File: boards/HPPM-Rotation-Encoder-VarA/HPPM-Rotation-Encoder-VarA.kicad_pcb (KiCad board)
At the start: 2 copper layers, 15 x 31.2 mm, 13 parts, among them J1 CONN, U1 AS5045B, U2 DS9638

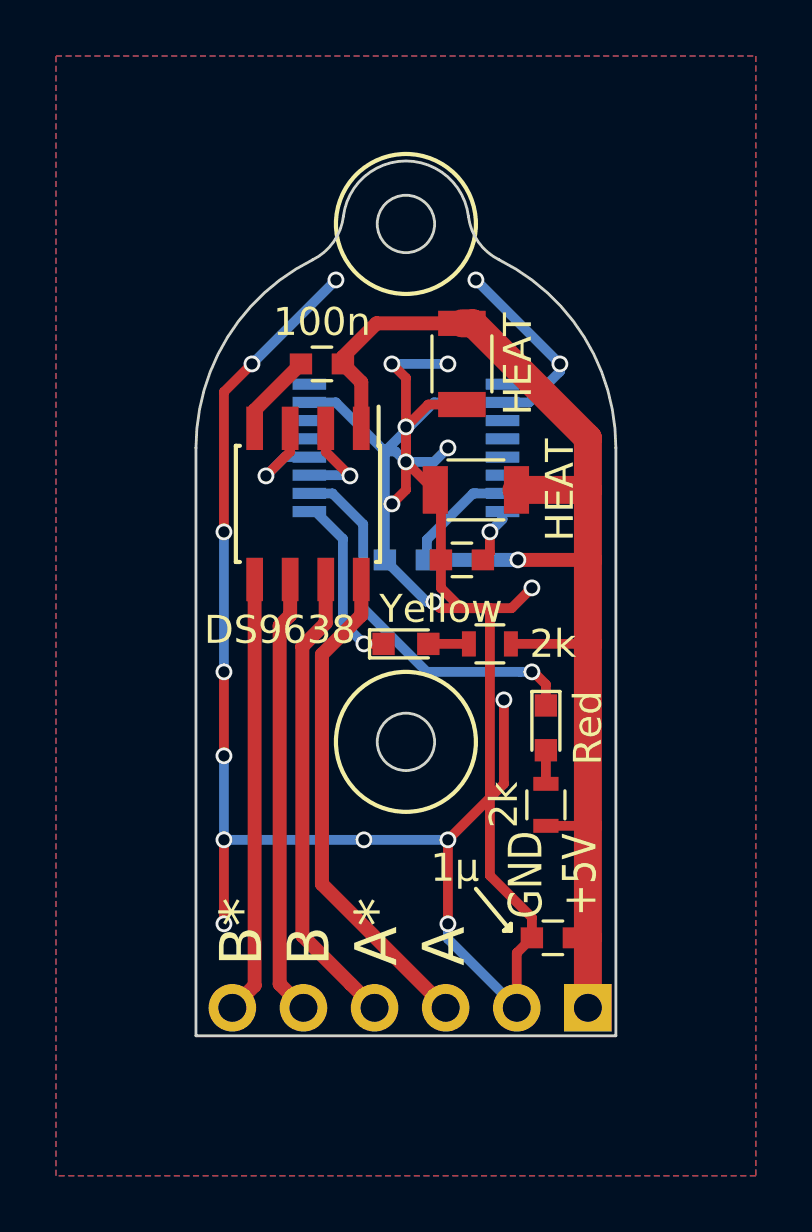
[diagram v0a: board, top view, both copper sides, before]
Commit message: [board][HPPM-Rotation-Encoder-VarA] fix wrong pinout
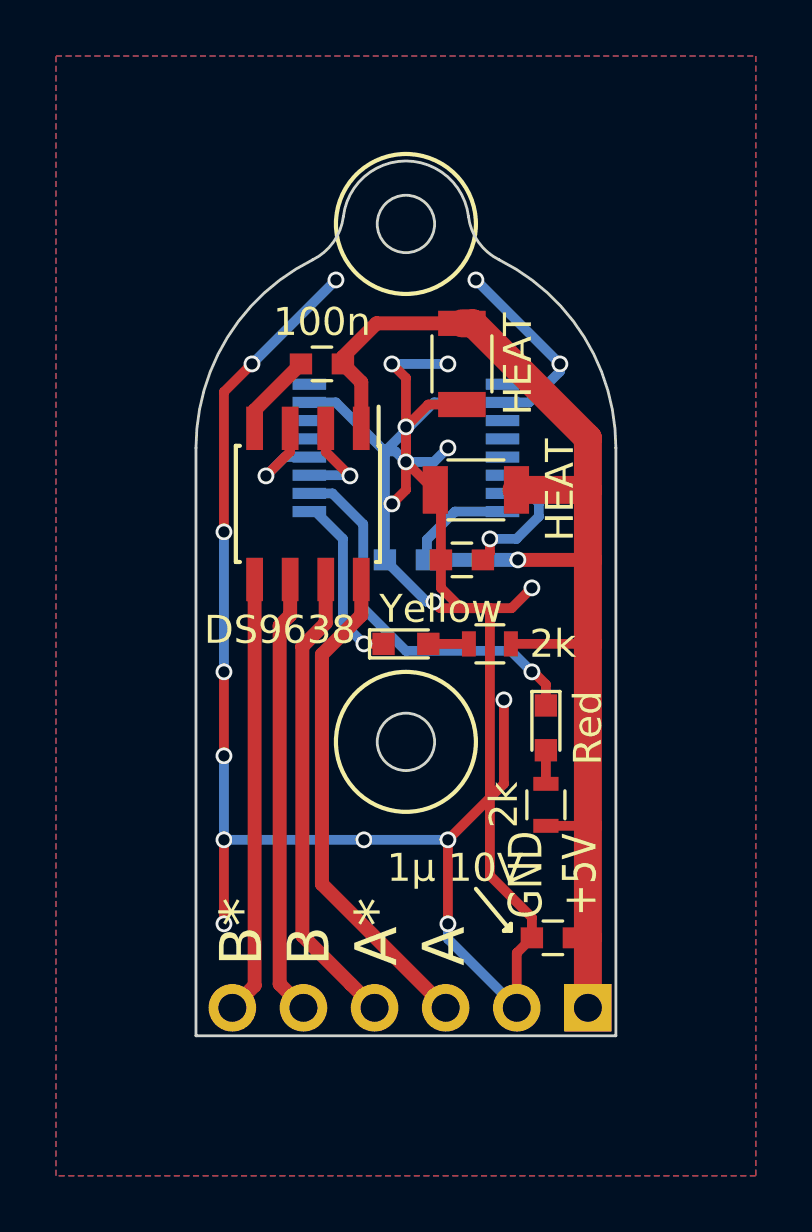
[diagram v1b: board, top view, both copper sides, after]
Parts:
- C4: value 1µ -> 1µ 10V
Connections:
- U1 pad 15: +5V -> Net-(C2-Pad1)
- U1 pad 16: Net-(C2-Pad1) -> +5V
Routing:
- net Net-(C2-Pad1): track 2.01 -> 4.85 mm
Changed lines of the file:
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@@
   (general
     (links 29)
-    (no_connects 0)
+    (no_connects 2)
     (area 49.949999 33.699999 65.050001 65.050001)
     (thickness 1.6)
     (drawings 23)
-    (tracks 150)
+    (tracks 152)
     (zones 0)
     (modules 13)
@@
   )
   (setup
-    (last_trace_width 0.25)
+    (last_trace_width 0.35)
     (user_trace_width 0.35)
     (user_trace_width 0.5)
@@
       (effects (font (size 1 1) (thickness 0.15)))
     )
-    (fp_text value 1µ (at 3.5 2.5 180) (layer F.SilkS)
+    (fp_text value "1µ 10V" (at 3.5 2.5 180) (layer F.SilkS)
       (effects (font (size 1 1) (thickness 0.15)))
     )
@@
     (pad 14 smd rect (at 3.45 0.975) (size 1.2 0.4) (layers B.Cu B.Paste B.Mask))
     (pad 15 smd rect (at 3.45 1.625) (size 1.2 0.4) (layers B.Cu B.Paste B.Mask)
-      (net 1 +5V))
+      (net 3 "Net-(C2-Pad1)"))
     (pad 16 smd rect (at 3.45 2.275) (size 1.2 0.4) (layers B.Cu B.Paste B.Mask)
-      (net 3 "Net-(C2-Pad1)"))
+      (net 1 +5V))
     (model Housings_SSOP.3dshapes/SSOP-16_5.3x6.2mm_Pitch0.65mm.wrl
       (at (xyz 0 0 0))
@@
   (gr_line (start 57.5 44) (end 52.5 44) (layer Dwgs.User) (width 0.1))
   (gr_line (start 50 65) (end 50 44) (layer Edge.Cuts) (width 0.1))
+  (segment (start 60.95 46.275) (end 59.25 46.275) (width 0.35) (layer B.Cu) (net 1))
+  (segment (start 59.25 46.275) (end 58.25 47.275) (width 0.35) (layer B.Cu) (net 1))
+  (segment (start 58.25 47.275) (end 58.25 48) (width 0.35) (layer B.Cu) (net 1))
   (segment (start 61.5 48) (end 58.25 48) (width 0.5) (layer B.Cu) (net 1))
   (via (at 61.5 48) (size 0.6) (drill 0.4) (layers F.Cu B.Cu) (net 1))
@@
   (segment (start 64 51) (end 64 48) (width 1) (layer F.Cu) (net 1))
   (segment (start 64 48) (end 64 45.5) (width 1) (layer F.Cu) (net 1))
-  (segment (start 58.25 48) (end 58.25 47.275) (width 0.35) (layer B.Cu) (net 1))
-  (segment (start 58.25 47.275) (end 59.9 45.625) (width 0.35) (layer B.Cu) (net 1))
-  (segment (start 59.9 45.625) (end 60 45.625) (width 0.35) (layer B.Cu) (net 1))
-  (segment (start 60 45.625) (end 60.95 45.625) (width 0.35) (layer B.Cu) (net 1))
   (segment (start 64 64) (end 64 61.5) (width 1) (layer F.Cu) (net 1))
   (segment (start 64 61.5) (end 64 57.5) (width 1) (layer F.Cu) (net 1))
@@
   (segment (start 52.095 43.3) (end 52.095 42.655) (width 0.5) (layer F.Cu) (net 2))
   (segment (start 52.095 42.655) (end 53.75 41) (width 0.5) (layer F.Cu) (net 2))
-  (segment (start 60.5 47) (end 60.5 47.75) (width 0.35) (layer F.Cu) (net 3))
+  (segment (start 60.5 47.25) (end 60.5 47.75) (width 0.35) (layer F.Cu) (net 3))
   (segment (start 60.5 47.75) (end 60.25 48) (width 0.35) (layer F.Cu) (net 3))
-  (segment (start 60.95 46.275) (end 60.95 46.55) (width 0.35) (layer B.Cu) (net 3))
-  (segment (start 60.95 46.55) (end 60.5 47) (width 0.35) (layer B.Cu) (net 3))
-  (via (at 60.5 47) (size 0.6) (drill 0.4) (layers F.Cu B.Cu) (net 3))
+  (segment (start 62.25 45.975) (end 62.25 46.450002) (width 0.35) (layer B.Cu) (net 3))
+  (segment (start 62.25 46.450002) (end 61.450002 47.25) (width 0.35) (layer B.Cu) (net 3))
+  (segment (start 61.450002 47.25) (end 60.5 47.25) (width 0.35) (layer B.Cu) (net 3))
+  (via (at 60.5 47.25) (size 0.6) (drill 0.4) (layers F.Cu B.Cu) (net 3))
+  (segment (start 60.95 45.625) (end 61.9 45.625) (width 0.35) (layer B.Cu) (net 3))
+  (segment (start 61.9 45.625) (end 62.25 45.975) (width 0.35) (layer B.Cu) (net 3))
   (segment (start 58.3 51) (end 59.75 51) (width 0.35) (layer F.Cu) (net 4))
   (segment (start 54.05 46.275) (end 54.275 46.275) (width 0.35) (layer B.Cu) (net 5))
@@
   (segment (start 54.05 45.625) (end 54.875 45.625) (width 0.35) (layer B.Cu) (net 7))
   (segment (start 54.875 45.625) (end 55.974999 46.724999) (width 0.35) (layer B.Cu) (net 7))
-  (segment (start 58.25 52) (end 61.575736 52) (width 0.35) (layer B.Cu) (net 7))
   (segment (start 55.974999 46.724999) (end 55.974999 49.724999) (width 0.35) (layer B.Cu) (net 7))
-  (segment (start 55.974999 49.724999) (end 58.25 52) (width 0.35) (layer B.Cu) (net 7))
-  (segment (start 61.575736 52) (end 62 52) (width 0.35) (layer B.Cu) (net 7))
+  (segment (start 55.974999 49.724999) (end 57.5 51.25) (width 0.35) (layer B.Cu) (net 7))
+  (segment (start 57.5 51.25) (end 61.25 51.25) (width 0.35) (layer B.Cu) (net 7))
+  (segment (start 61.25 51.25) (end 62 52) (width 0.35) (layer B.Cu) (net 7))
   (segment (start 62.05 52) (end 62 52) (width 0.35) (layer F.Cu) (net 7))
   (segment (start 62.5 52.45) (end 62.05 52) (width 0.35) (layer F.Cu) (net 7))
@@
     (min_thickness 0.25)
     (keepout (tracks not_allowed) (vias not_allowed) (copperpour not_allowed))
-    (fill (arc_segments 16) (thermal_gap 0.25) (thermal_bridge_width 0.3))
+    (fill yes (arc_segments 16) (thermal_gap 0.25) (thermal_bridge_width 0.3))
     (polygon
       (pts

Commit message: [board][HPPM-Rotation-Encoder-Var*] minor fiixes: DRC and PDIO wired to GND
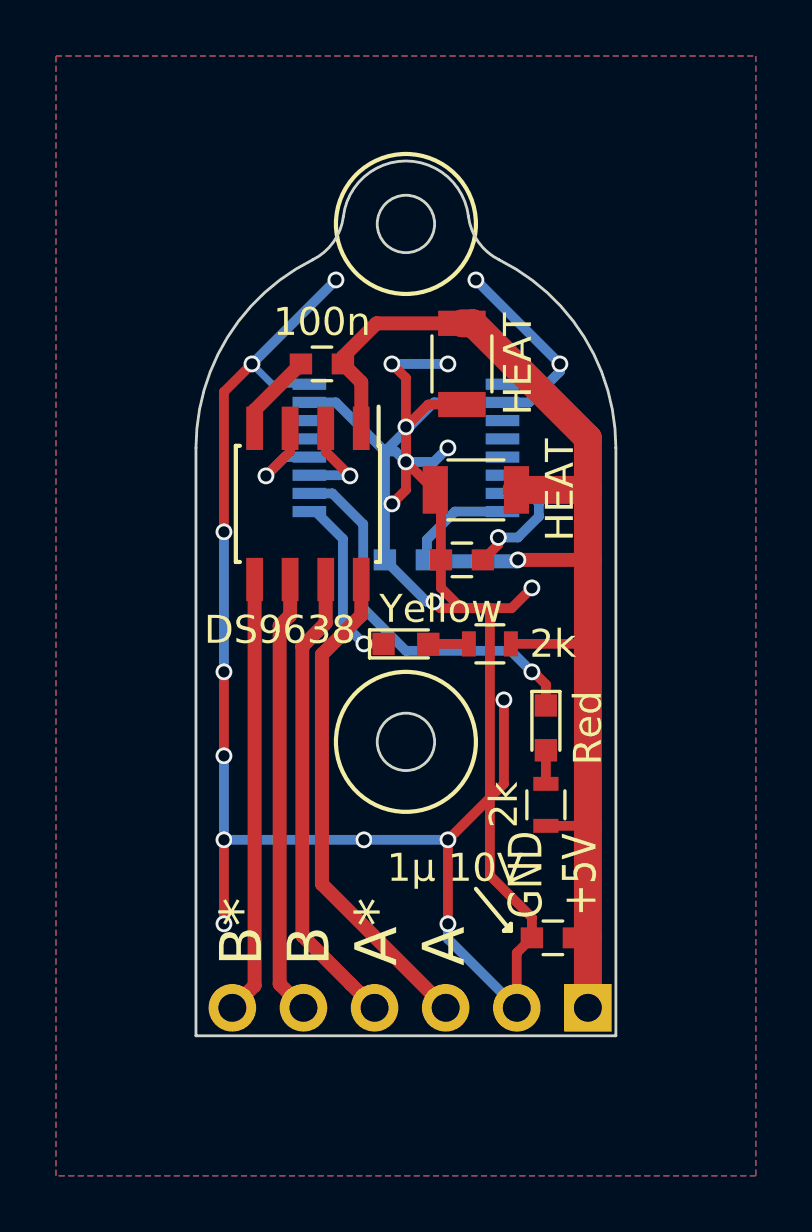
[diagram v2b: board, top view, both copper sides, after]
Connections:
- U1 pad 8: (no net) -> GND
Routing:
- net GND: track 111.1 -> 113.4 mm
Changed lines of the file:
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@@
-(kicad_pcb (version 4) (host pcbnew 4.0.6)
+(kicad_pcb (version 4) (host pcbnew 4.0.7)
   (general
-    (links 29)
-    (no_connects 2)
-    (area 49.949999 33.699999 65.050001 65.050001)
+    (links 30)
+    (no_connects 0)
+    (area 45 30 70.000001 70.000001)
     (thickness 1.6)
     (drawings 23)
-    (tracks 152)
+    (tracks 156)
     (zones 0)
     (modules 13)
@@
   )
   (setup
-    (last_trace_width 0.35)
+    (last_trace_width 0.25)
     (user_trace_width 0.35)
     (user_trace_width 0.5)
@@
     (pad 7 smd rect (at -3.45 -1.625) (size 1.2 0.4) (layers B.Cu B.Paste B.Mask)
       (net 2 GND))
-    (pad 8 smd rect (at -3.45 -2.275) (size 1.2 0.4) (layers B.Cu B.Paste B.Mask))
+    (pad 8 smd rect (at -3.45 -2.275) (size 1.2 0.4) (layers B.Cu B.Paste B.Mask)
+      (net 2 GND))
     (pad 9 smd rect (at 3.45 -2.275) (size 1.2 0.4) (layers B.Cu B.Paste B.Mask))
     (pad 10 smd rect (at 3.45 -1.625) (size 1.2 0.4) (layers B.Cu B.Paste B.Mask)
@@
   (gr_line (start 57.5 44) (end 52.5 44) (layer Dwgs.User) (width 0.1))
   (gr_line (start 50 65) (end 50 44) (layer Edge.Cuts) (width 0.1))
+  (segment (start 61.5 48) (end 61.449999 48.050001) (width 0.5) (layer B.Cu) (net 1))
+  (segment (start 61.449999 48.050001) (end 58.300001 48.050001) (width 0.5) (layer B.Cu) (net 1))
+  (segment (start 58.300001 48.050001) (end 58.25 48) (width 0.5) (layer B.Cu) (net 1))
   (segment (start 60.95 46.275) (end 59.25 46.275) (width 0.35) (layer B.Cu) (net 1))
   (segment (start 59.25 46.275) (end 58.25 47.275) (width 0.35) (layer B.Cu) (net 1))
   (segment (start 58.25 47.275) (end 58.25 48) (width 0.35) (layer B.Cu) (net 1))
-  (segment (start 61.5 48) (end 58.25 48) (width 0.5) (layer B.Cu) (net 1))
   (via (at 61.5 48) (size 0.6) (drill 0.4) (layers F.Cu B.Cu) (net 1))
   (segment (start 64 48) (end 61.5 48) (width 0.5) (layer F.Cu) (net 1))
@@
   (segment (start 55.905 43.3) (end 55.905 41.655) (width 0.5) (layer F.Cu) (net 1))
   (segment (start 55.905 41.655) (end 55.25 41) (width 0.5) (layer F.Cu) (net 1))
+  (segment (start 54.05 41.725) (end 52.725 41.725) (width 0.25) (layer B.Cu) (net 2))
+  (segment (start 52.725 41.725) (end 52 41) (width 0.25) (layer B.Cu) (net 2))
   (segment (start 57.5 44.5) (end 57.5 43.25) (width 0.35) (layer F.Cu) (net 2))
   (via (at 57.5 43.25) (size 0.6) (drill 0.4) (layers F.Cu B.Cu) (net 2))
@@
   (segment (start 52.095 43.3) (end 52.095 42.655) (width 0.5) (layer F.Cu) (net 2))
   (segment (start 52.095 42.655) (end 53.75 41) (width 0.5) (layer F.Cu) (net 2))
-  (segment (start 60.5 47.25) (end 60.5 47.75) (width 0.35) (layer F.Cu) (net 3))
-  (segment (start 60.5 47.75) (end 60.25 48) (width 0.35) (layer F.Cu) (net 3))
+  (segment (start 62.25 46.450002) (end 61.499996 47.200006) (width 0.35) (layer B.Cu) (net 3))
+  (segment (start 61.499996 47.200006) (end 60.8 47.200006) (width 0.35) (layer B.Cu) (net 3))
   (segment (start 62.25 45.975) (end 62.25 46.450002) (width 0.35) (layer B.Cu) (net 3))
-  (segment (start 62.25 46.450002) (end 61.450002 47.25) (width 0.35) (layer B.Cu) (net 3))
-  (segment (start 61.450002 47.25) (end 60.5 47.25) (width 0.35) (layer B.Cu) (net 3))
-  (via (at 60.5 47.25) (size 0.6) (drill 0.4) (layers F.Cu B.Cu) (net 3))
   (segment (start 60.95 45.625) (end 61.9 45.625) (width 0.35) (layer B.Cu) (net 3))
+  (segment (start 60.8 47.45) (end 60.8 47.200006) (width 0.35) (layer F.Cu) (net 3))
+  (segment (start 60.25 48) (end 60.8 47.45) (width 0.35) (layer F.Cu) (net 3))
+  (via (at 60.8 47.200006) (size 0.6) (drill 0.4) (layers F.Cu B.Cu) (net 3))
   (segment (start 61.9 45.625) (end 62.25 45.975) (width 0.35) (layer B.Cu) (net 3))
   (segment (start 58.3 51) (end 59.75 51) (width 0.35) (layer F.Cu) (net 4))
